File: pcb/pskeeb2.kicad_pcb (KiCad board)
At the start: 2 copper layers, 98 x 91.5 mm, 29 parts, among them K11 KEYSW, K12 KEYSW, K13 KEYSW, K14 KEYSW, K15 KEYSW, K21 KEYSW, K22 KEYSW, K23 KEYSW, K24 KEYSW, K25 KEYSW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

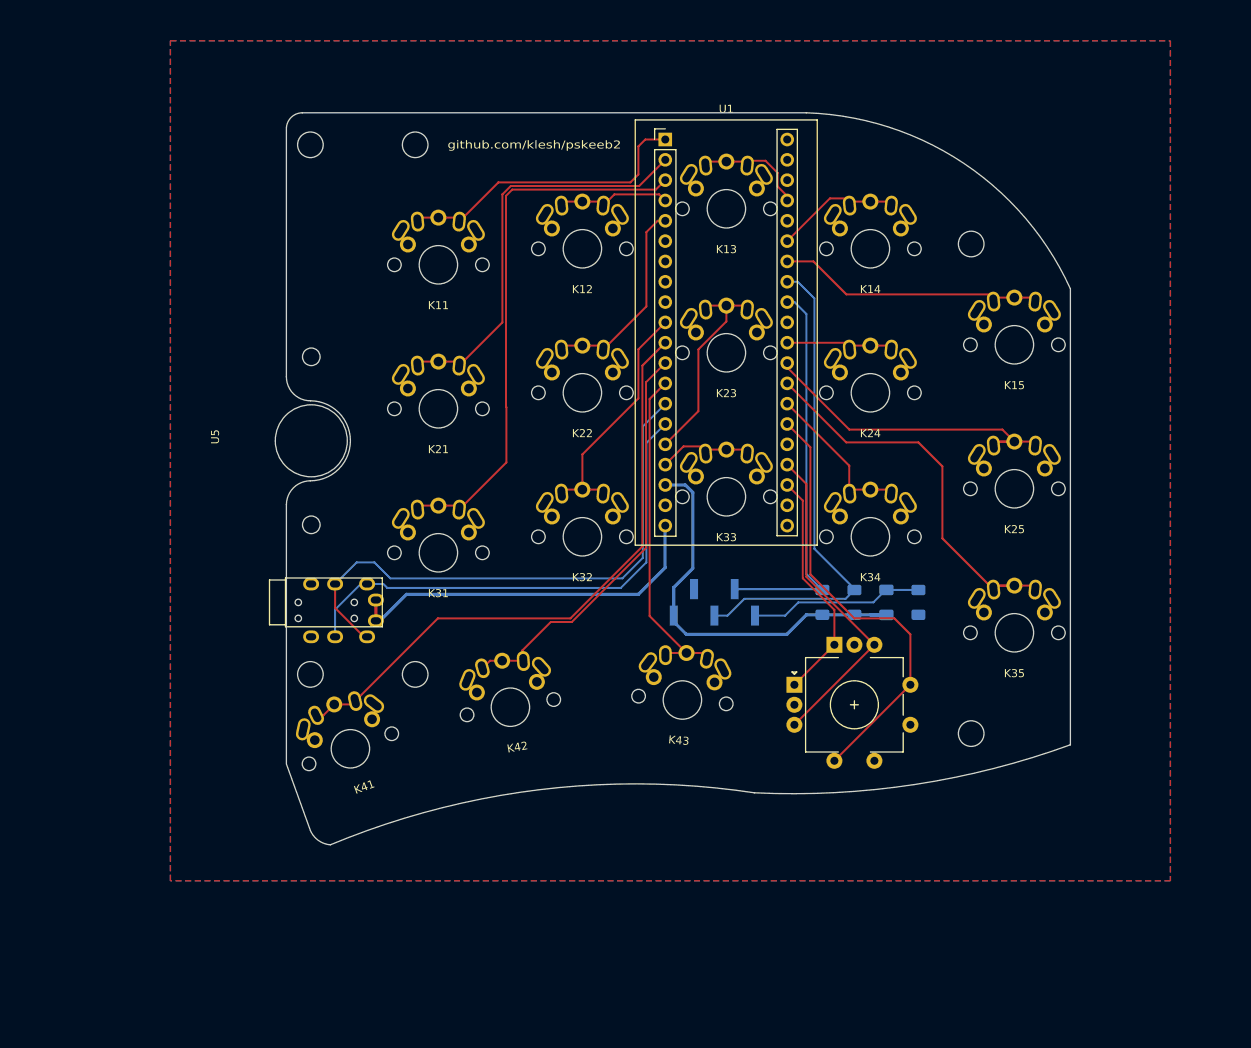
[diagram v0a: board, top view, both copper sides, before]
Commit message: fix: switch courtyard too small / trackpoint mounting
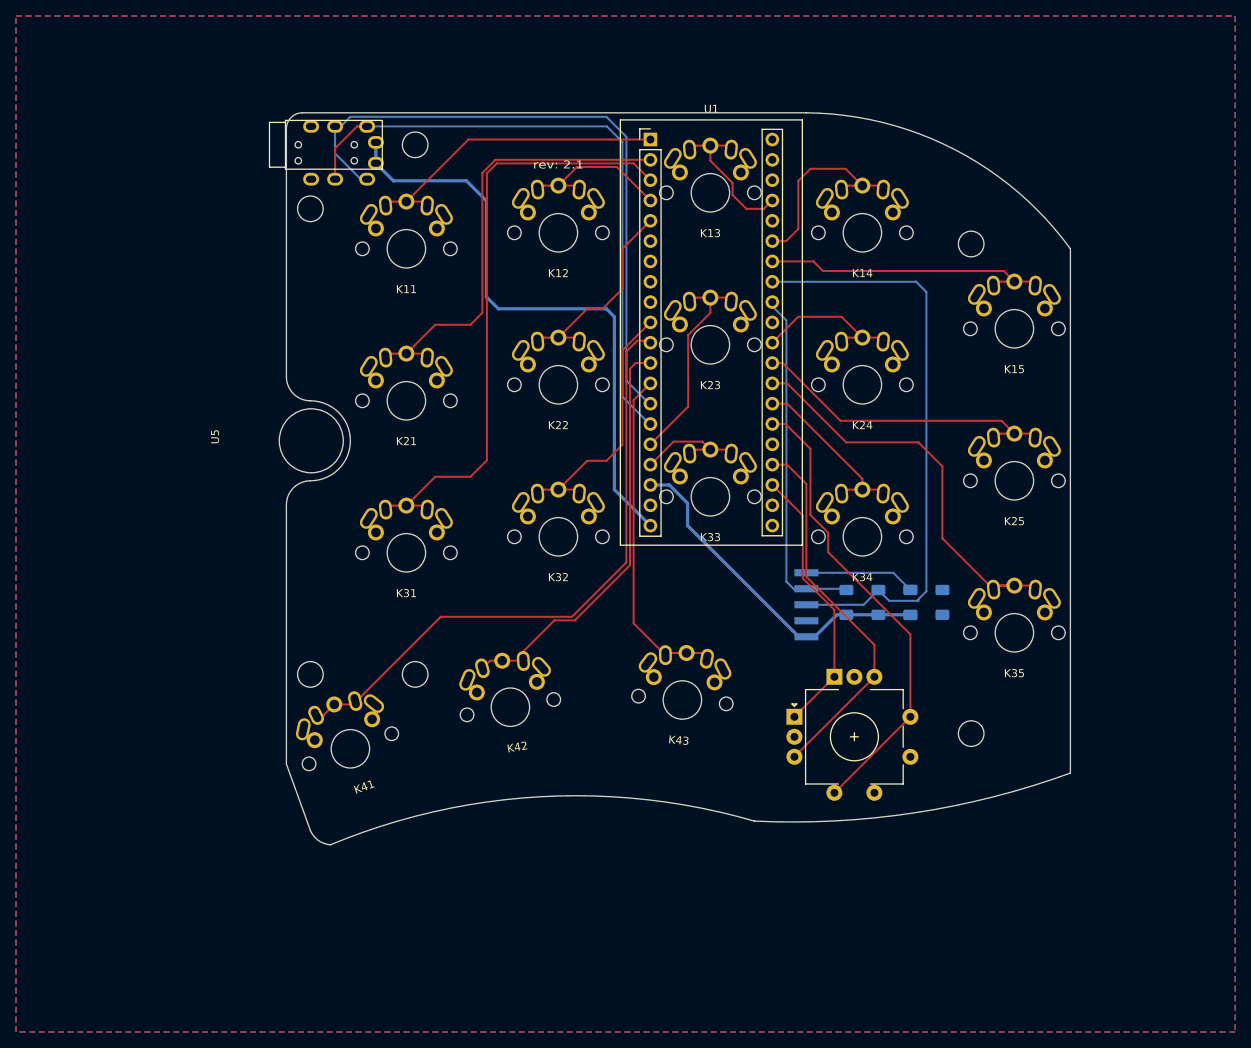
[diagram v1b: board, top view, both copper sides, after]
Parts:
- U4: footprint Connector_PinHeader_2.54mm:PinHeader_1x05_P2.54mm_Vertical_SMD_Pin1Left -> kwkb-footprint:HY20_1x05_P2.00mm_Vertical_SMD
- U5: footprint kwkb-footprint:T400-Trackpoint -> kwkb-footprint:T400-Trackpoint-mix
- moved U2 57.2 mm to (81.4, 37.0)
- moved U3 57.2 mm to (81.4, 39.0)
- moved U4 8.01 mm to (143.0, 94.5), turned to 180 degrees
- moved K11 4.47 mm to (96.5, 50.0)
- moved K21 4.12 mm to (96.5, 69.0)
- moved K31 4.00 mm to (96.5, 88.0)
- moved SW1 4.00 mm to (152.5, 111.0)
- moved SW2 4.00 mm to (152.5, 111.0)
- moved K12 3.61 mm to (115.5, 48.0)
- moved K22 3.16 mm to (115.5, 67.0)
- moved C1 3.00 mm to (159.5, 94.2)
- moved K32 3.00 mm to (115.5, 86.0)
- moved R1 3.00 mm to (155.5, 94.2)
- moved R2 3.00 mm to (151.5, 94.2)
- moved R3 3.00 mm to (163.5, 94.2)
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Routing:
- net +3V3: track 46.8 -> 75.4 mm
- net RX: track 63.4 -> 78.7 mm
- net TP_CLK: track 61.6 -> 74.1 mm
- net TX: track 70.4 -> 81.5 mm
- net TP_RST: track 23.8 -> 13.9 mm
- net /k14: track 15.8 -> 25.0 mm
- net +5V: track 51.2 -> 43.1 mm
- net /k31: track 68.0 -> 75.7 mm
- net TP_DAT: track 49.1 -> 42.4 mm
- net /k24: track 13.6 -> 19.6 mm
- net ENB: track 41.2 -> 47.0 mm
- net /k12: track 14.3 -> 19.8 mm
- net /k13: track 14.4 -> 19.3 mm
- net ENA: track 29.5 -> 34.3 mm
- net /k15: track 33.3 -> 37.9 mm
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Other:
- outline, holes or cut-outs redrawn
- board text added: "rev: 2.1"
- board text removed: "github.com/klesh/pskeeb2"
